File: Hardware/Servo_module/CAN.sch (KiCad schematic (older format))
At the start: 2 parts

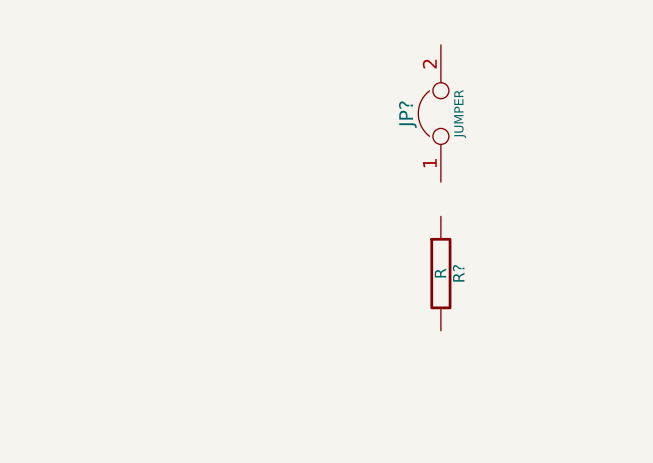
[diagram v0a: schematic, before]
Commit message: [HARDWARE][SERVO_MODULE] Schematic
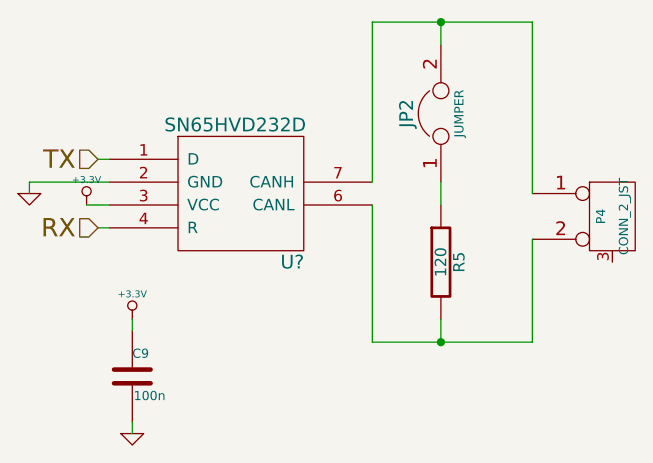
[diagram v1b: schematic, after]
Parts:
- added C9: 100n, ~, symbol C
- added P4: CONN_2_JST, symbol CONN_2_JST
- added U?: SN65HVD232D, symbol SN65HVD232D
- R5: renamed from R?; value R -> 120
- gave numbers to parts that had none: 1
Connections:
- net at JP2.1: now also R5.1
- net at JP2.2: now also P4.1 (P1), U?.7 (CANH)
- net at R5.2: now also P4.2 (PM), U?.6 (CANL)
- new net +3.3V: C9.1, U?.3 (VCC)
- new net GND: C9.2, U?.2 (GND)
- new net RX: U?.4 (R)
- new net TX: U?.1 (D)
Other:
- moved on the sheet: R5
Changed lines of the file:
@@
-EESchema Schematic File Version 2  date Fri 18 Oct 2013 03:55:13 PM CEST
+EESchema Schematic File Version 2
 LIBS:power
 LIBS:device
@@
 LIBS:conn_2_jst
 LIBS:conn_4_jst
+LIBS:sn65hvd232d
 LIBS:serv_module-cache
-EELAYER 24  0
+EELAYER 27 0
 EELAYER END
-$Descr A4 11700 8267
-Sheet 2 4
+$Descr A4 11693 8268
+encoding utf-8
+Sheet 3 4
 Title ""
-Date "18 oct 2013"
+Date "25 oct 2013"
 Rev ""
 Comp ""
@@
 $EndDescr
 $Comp
-L R R?
+L R R5
 U 1 1 52612F7A
-P 4750 4100
-F 0 "R?" V 4830 4100 50  0000 C CNN
-F 1 "R" V 4750 4100 50  0000 C CNN
-	1    4750 4100
+P 4750 4050
+F 0 "R5" V 4830 4050 50  0000 C CNN
+F 1 "120" V 4750 4050 50  0000 C CNN
+F 2 "" H 4750 4050 60  0001 C CNN
+F 3 "" H 4750 4050 60  0001 C CNN
+	1    4750 4050
 	1    0    0    -1
 $EndComp
 $Comp
-L JUMPER JP?
+L JUMPER JP2
 U 1 1 52612EF3
 P 4750 3400
-F 0 "JP?" H 4750 3550 60  0000 C CNN
+F 0 "JP2" H 4750 3550 60  0000 C CNN
 F 1 "JUMPER" H 4750 3320 40  0000 C CNN
+F 2 "" H 4750 3400 60  0001 C CNN
+F 3 "" H 4750 3400 60  0001 C CNN
 	1    4750 3400
 	0    -1   -1   0
 $EndComp
+$Comp
+L SN65HVD232D U?
+U 1 1 526A2A55
+P 3850 3750
+F 0 "U?" H 4100 3450 60  0000 C CNN
+F 1 "SN65HVD232D" H 3850 4050 60  0000 C CNN
+F 2 "" H 3850 3750 60  0000 C CNN
+F 3 "" H 3850 3750 60  0000 C CNN
+	1    3850 3750
+	1    0    0    -1
+$EndComp
+Wire Wire Line
+	4750 3700 4750 3800
+Wire Wire Line
+	4450 3700 4450 3000
+Wire Wire Line
+	4450 3000 5150 3000
+Wire Wire Line
+	4750 3000 4750 3100
+Wire Wire Line
+	4450 3800 4450 4400
+Wire Wire Line
+	4450 4400 5150 4400
+Wire Wire Line
+	4750 4400 4750 4300
+$Comp
+L GND #PWR?
+U 1 1 526A2AB5
+P 2950 3750
+F 0 "#PWR?" H 2950 3750 30  0001 C CNN
+F 1 "GND" H 2950 3680 30  0001 C CNN
+F 2 "" H 2950 3750 60  0000 C CNN
+F 3 "" H 2950 3750 60  0000 C CNN
+	1    2950 3750
+	1    0    0    -1
+$EndComp
+$Comp
+L CONN_2_JST P4
+U 1 1 526A2AC4
+P 5500 3850
+F 0 "P4" V 5450 3850 40  0000 C CNN
+F 1 "CONN_2_JST" V 5550 3850 40  0000 C CNN
+F 2 "" H 5500 3850 60  0000 C CNN
+F 3 "" H 5500 3850 60  0000 C CNN
+	1    5500 3850
+	1    0    0    -1
+$EndComp
+Wire Wire Line
+	3300 3700 2950 3700
+Wire Wire Line
+	2950 3700 2950 3750
+$Comp
+L +3.3V #PWR?
+U 1 1 526A2B0C
+P 3200 3800
+F 0 "#PWR?" H 3200 3760 30  0001 C CNN
+F 1 "+3.3V" H 3200 3910 30  0000 C CNN
+F 2 "" H 3200 3800 60  0000 C CNN
+F 3 "" H 3200 3800 60  0000 C CNN
+	1    3200 3800
+	1    0    0    -1
+$EndComp
+Wire Wire Line
+	3200 3800 3300 3800
+Wire Wire Line
+	3300 3600 3250 3600
+Wire Wire Line
+	3300 3900 3250 3900
+Text HLabel 3250 3600 0    80   Input ~ 0
+TX
+Text HLabel 3250 3900 0    80   Input ~ 0
+RX
+Wire Wire Line
+	5150 4400 5150 3950
+Connection ~ 4750 4400
+Wire Wire Line
+	5150 3000 5150 3750
+Connection ~ 4750 3000
+$Comp
+L +3.3V #PWR?
+U 1 1 526A2B62
+P 3400 4300
+F 0 "#PWR?" H 3400 4260 30  0001 C CNN
+F 1 "+3.3V" H 3400 4410 30  0000 C CNN
+F 2 "" H 3400 4300 60  0000 C CNN
+F 3 "" H 3400 4300 60  0000 C CNN
+	1    3400 4300
+	1    0    0    -1
+$EndComp
+$Comp
+L C C9
+U 1 1 526A2B6A
+P 3400 4550
+F 0 "C9" H 3400 4650 40  0000 L CNN
+F 1 "100n" H 3406 4465 40  0000 L CNN
+F 2 "~" H 3438 4400 30  0000 C CNN
+F 3 "~" H 3400 4550 60  0000 C CNN
+	1    3400 4550
+	1    0    0    -1
+$EndComp
+Wire Wire Line
+	3400 4300 3400 4350
+$Comp
+L GND #PWR?
+U 1 1 526A2B94
+P 3400 4800
+F 0 "#PWR?" H 3400 4800 30  0001 C CNN
+F 1 "GND" H 3400 4730 30  0001 C CNN
+F 2 "" H 3400 4800 60  0000 C CNN
+F 3 "" H 3400 4800 60  0000 C CNN
+	1    3400 4800
+	1    0    0    -1
+$EndComp
+Wire Wire Line
+	3400 4750 3400 4800
 $EndSCHEMATC

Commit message: [HARDWARE][SERVO_MODULE] Schematic
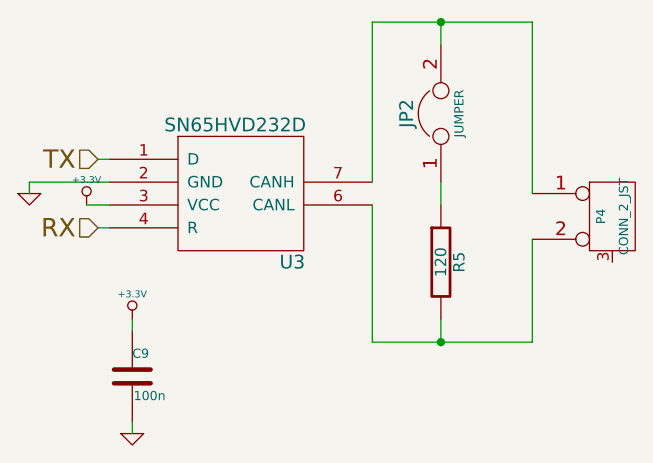
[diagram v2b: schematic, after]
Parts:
- gave numbers to parts that had none: 1
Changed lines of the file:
@@
 $EndComp
 $Comp
-L SN65HVD232D U?
+L SN65HVD232D U3
 U 1 1 526A2A55
 P 3850 3750
-F 0 "U?" H 4100 3450 60  0000 C CNN
+F 0 "U3" H 4100 3450 60  0000 C CNN
 F 1 "SN65HVD232D" H 3850 4050 60  0000 C CNN
 F 2 "" H 3850 3750 60  0000 C CNN
@@
 	4750 4400 4750 4300
 $Comp
-L GND #PWR?
+L GND #PWR06
 U 1 1 526A2AB5
 P 2950 3750
-F 0 "#PWR?" H 2950 3750 30  0001 C CNN
+F 0 "#PWR06" H 2950 3750 30  0001 C CNN
 F 1 "GND" H 2950 3680 30  0001 C CNN
 F 2 "" H 2950 3750 60  0000 C CNN
@@
 	2950 3700 2950 3750
 $Comp
-L +3.3V #PWR?
+L +3.3V #PWR07
 U 1 1 526A2B0C
 P 3200 3800
-F 0 "#PWR?" H 3200 3760 30  0001 C CNN
+F 0 "#PWR07" H 3200 3760 30  0001 C CNN
 F 1 "+3.3V" H 3200 3910 30  0000 C CNN
 F 2 "" H 3200 3800 60  0000 C CNN
@@
 Connection ~ 4750 3000
 $Comp
-L +3.3V #PWR?
+L +3.3V #PWR08
 U 1 1 526A2B62
 P 3400 4300
-F 0 "#PWR?" H 3400 4260 30  0001 C CNN
+F 0 "#PWR08" H 3400 4260 30  0001 C CNN
 F 1 "+3.3V" H 3400 4410 30  0000 C CNN
 F 2 "" H 3400 4300 60  0000 C CNN
@@
 	3400 4300 3400 4350
 $Comp
-L GND #PWR?
+L GND #PWR09
 U 1 1 526A2B94
 P 3400 4800
-F 0 "#PWR?" H 3400 4800 30  0001 C CNN
+F 0 "#PWR09" H 3400 4800 30  0001 C CNN
 F 1 "GND" H 3400 4730 30  0001 C CNN
 F 2 "" H 3400 4800 60  0000 C CNN

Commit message: [HARDWARE][SERVO_MODULE] Update schemating & routing
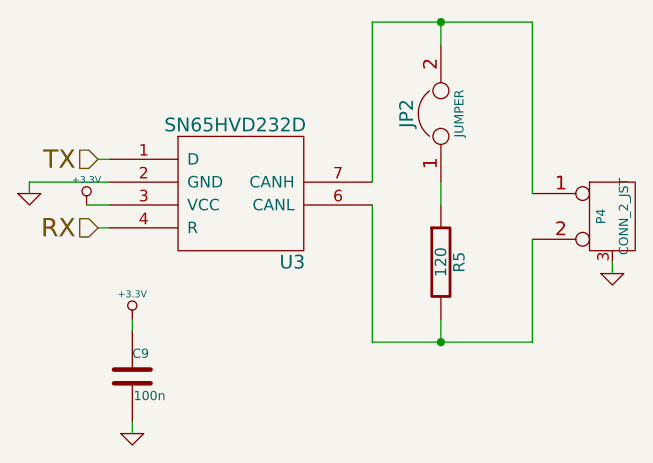
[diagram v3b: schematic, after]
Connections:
- net GND: now also P4.3
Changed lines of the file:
@@
 LIBS:contrib
 LIBS:valves
-LIBS:stm32f103c4
 LIBS:ap1117
 LIBS:conn_2_jst
 LIBS:conn_4_jst
 LIBS:sn65hvd232d
+LIBS:stm32f103c4
 LIBS:serv_module-cache
 EELAYER 27 0
@@
 $Descr A4 11693 8268
 encoding utf-8
-Sheet 3 4
+Sheet 2 4
 Title ""
 Date "25 oct 2013"
@@
 	4750 4400 4750 4300
 $Comp
-L GND #PWR06
+L GND #PWR01
 U 1 1 526A2AB5
 P 2950 3750
-F 0 "#PWR06" H 2950 3750 30  0001 C CNN
+F 0 "#PWR01" H 2950 3750 30  0001 C CNN
 F 1 "GND" H 2950 3680 30  0001 C CNN
 F 2 "" H 2950 3750 60  0000 C CNN
@@
 	2950 3700 2950 3750
 $Comp
-L +3.3V #PWR07
+L +3.3V #PWR02
 U 1 1 526A2B0C
 P 3200 3800
-F 0 "#PWR07" H 3200 3760 30  0001 C CNN
+F 0 "#PWR02" H 3200 3760 30  0001 C CNN
 F 1 "+3.3V" H 3200 3910 30  0000 C CNN
 F 2 "" H 3200 3800 60  0000 C CNN
@@
 Connection ~ 4750 3000
 $Comp
-L +3.3V #PWR08
+L +3.3V #PWR03
 U 1 1 526A2B62
 P 3400 4300
-F 0 "#PWR08" H 3400 4260 30  0001 C CNN
+F 0 "#PWR03" H 3400 4260 30  0001 C CNN
 F 1 "+3.3V" H 3400 4410 30  0000 C CNN
 F 2 "" H 3400 4300 60  0000 C CNN
@@
 	3400 4300 3400 4350
 $Comp
-L GND #PWR09
+L GND #PWR04
 U 1 1 526A2B94
 P 3400 4800
-F 0 "#PWR09" H 3400 4800 30  0001 C CNN
+F 0 "#PWR04" H 3400 4800 30  0001 C CNN
 F 1 "GND" H 3400 4730 30  0001 C CNN
 F 2 "" H 3400 4800 60  0000 C CNN
@@
 Wire Wire Line
 	3400 4750 3400 4800
+$Comp
+L GND #PWR05
+U 1 1 526AA067
+P 5500 4100
+F 0 "#PWR05" H 5500 4100 30  0001 C CNN
+F 1 "GND" H 5500 4030 30  0001 C CNN
+F 2 "" H 5500 4100 60  0000 C CNN
+F 3 "" H 5500 4100 60  0000 C CNN
+	1    5500 4100
+	1    0    0    -1
+$EndComp
+Wire Wire Line
+	5500 4050 5500 4100
 $EndSCHEMATC
